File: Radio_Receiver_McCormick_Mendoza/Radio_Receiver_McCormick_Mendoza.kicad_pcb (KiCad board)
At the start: 4 copper layers, 100 x 100 mm, 243 parts, among them J1 VBAT, J10 CLK_2, J11 I_LO, J12 Q_LO, J13 I_0, J14 I_180, J15 Q_90, J16 Q_270, J17 I_RAW, J18 Conn_01x02_Female, J19 Conn_01x02_Female, J2 GND, J20 Q_RAW, J21 SDR Out, J23 VDDA, J24 CLK_0, J25 OLED, J26 +5V, J3 3.3VA, J33 XFIL_IN, J34 XFIL_OUT, J35 3.5mm_Jack, J36 +5RAW, J37 4.5V, J38 DAC_FLT, J39 VDD, J4 4.5VA, J40 DAC_FMT, J41 V_DIV, J42 VDDA/2, J45 CENTER_TAP, J46 3.5mm_Jack, J47 FIL_IN, J5 Conn_Coaxial, J6 Conn_01x02, J7 Micro_SD-TF_PUSH, J8 FIL_OUT, J9 CLK_1, SW1 RotaryEncoder_Switch_MP, SW6 09.03290.01, T1 Transformer_1P_SS, U1 TPS7A2045PDQN, U10 OPA1612AID, U11 INA821ID, U12 PCM1808PWR, U13 SN74CBT3253CDBR, U14 PCM5102A, U2 TPS7A2045PDQN, U3 TPS72733DSER, U4 Pico, U5 Si5351A-B-GT, U6 SN74AC74DR, U8 SN74CBT3253CDBR, U9 INA821ID, Y1 ASTX-H11-24.576MHZ-T

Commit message: Added netclasses for all the critical trace types
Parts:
- moved C32 15.6 mm to (103.6, 111.4)
- moved C33 15.6 mm to (100.2, 108.4)
- moved J23 15.6 mm to (100.0, 116.1)
- moved J3 15.6 mm to (96.6, 107.2)
- moved C12 15.6 mm to (104.7, 113.8)
- moved C1 15.6 mm to (104.3, 107.8)
- moved C6 15.6 mm to (99.8, 110.1)
- moved FB19 15.6 mm to (100.2, 106.8)
- moved J2 15.6 mm to (95.6, 110.8)
- moved J4 15.6 mm to (95.6, 114.6)
- moved U1 15.6 mm to (103.6, 109.8)
- moved U3 15.6 mm to (100.3, 112.7)
- moved C34 15.6 mm to (98.2, 112.8)
- moved FB18 15.6 mm to (102.7, 113.9)
- moved C22 3.69 mm to (78.4, 108.1), turned to 90 degrees

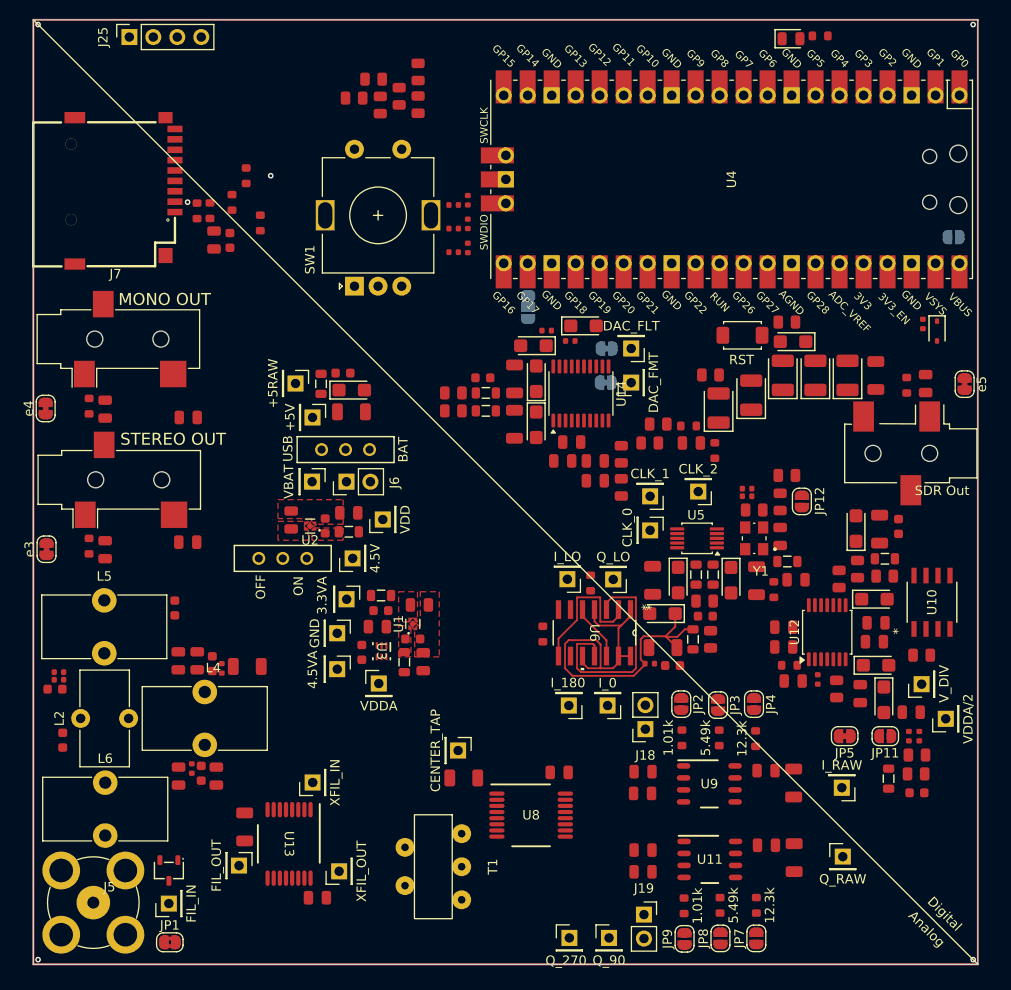
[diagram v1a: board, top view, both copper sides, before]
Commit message: Routed antenna and isolated GNDA
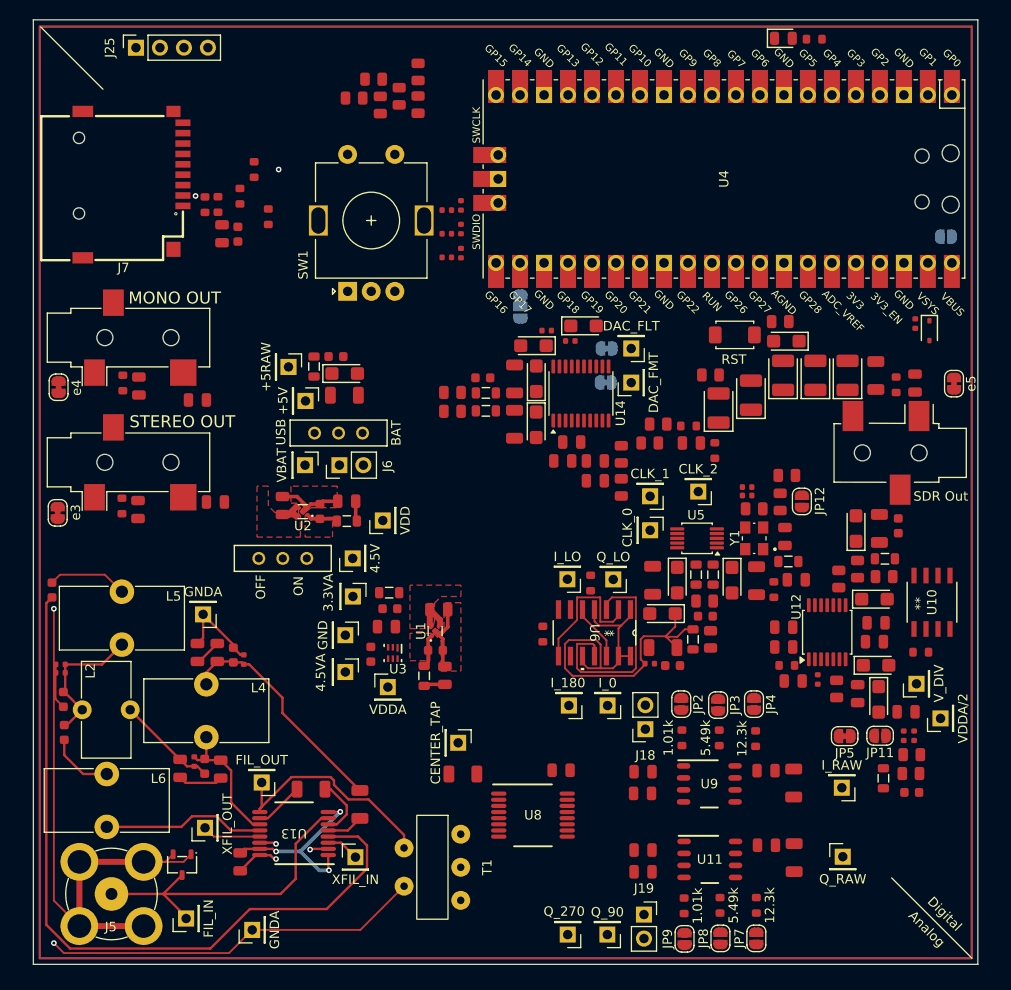
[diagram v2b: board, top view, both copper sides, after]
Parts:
- removed JP1: Jumper_NC_Small, Jumper:SolderJumper-2_P1.3mm_Bridged2Bar_RoundedPad1.0x1.5mm
- added J48: GNDA, Connector_PinHeader_2.54mm:PinHeader_1x01_P2.54mm_Vertical, F.Cu at (81.4, 108.8)
- added J49: GNDA, Connector_PinHeader_2.54mm:PinHeader_1x01_P2.54mm_Vertical, F.Cu at (86.6, 142.2)
- J7: footprint 0_Personal:TF-SMD_TF-PUSH -> Reciever_Parts:TF-SMD_TF-PUSH
- R5: value 22kΩ -> 22Ω; footprint PCM_JLCPCB:R_0805 -> PCM_JLCPCB:R_0603
- U11, U9: footprint INA821ID:D0008A_N -> Reciever_Parts:D0008A_N
- U13, U8: footprint SN74CBT3253CDBR_1-4_MUX:DB0016A_N -> Reciever_Parts:DB0016A_N
- U3: footprint TPS727-3.3V_regulator:DSE0006A -> Reciever_Parts:TS727_3.3VDSE0006A
- moved C67 18.9 mm to (98.0, 128.9), turned to 90 degrees
- moved J34 14.9 mm to (81.6, 131.4)
- moved C22 13.1 mm to (65.4, 106.2)
- moved J8 9.12 mm to (87.6, 126.6), turned to 180 degrees
- moved J33 9.10 mm to (97.5, 134.5), turned to 0 degrees
- moved C20 9.02 mm to (85.3, 135.0), turned to -90 degrees
- moved C61 8.08 mm to (92.8, 127.3), turned to 180 degrees
- moved C50 5.50 mm to (74.5, 97.7)
- moved R28 5.50 mm to (72.8, 97.3)
- moved C88 5.17 mm to (82.7, 96.9)
- moved R43 4.33 mm to (72.9, 84.3)
- moved C57 4.33 mm to (74.6, 84.6)
- moved e3 4.03 mm to (66.0, 98.0)
- moved C12 2.72 mm to (107.0, 115.3)
- moved C32 2.69 mm to (106.0, 112.6)
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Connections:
- net /ADC-24bit/VDDA/2 renamed /VREF
- net Net-(C11-Pad1) renamed /Antenna/LPF2
- net Net-(C2-Pad1) renamed /Antenna/BPF2
- net Net-(C42-Pad1) renamed /Audio DAC/OUTR_FIL
- net Net-(C43-Pad1) renamed /Audio DAC/OUTL_FIL
- net Net-(C47-Pad1) renamed /ADC-24bit/I_OUTA
- net Net-(C48-Pad1) renamed /ADC-24bit/Q_OUTA
- net Net-(C49-Pad1) renamed /Audio DAC/OUTLR
- net Net-(C59-Pad2) renamed /Audio DAC/MONO
- net Net-(C60-Pad2) renamed /Audio DAC/StereoR
- net Net-(C64-Pad1) renamed /Audio DAC/3.3VA
- net Net-(C70-Pad1) renamed /Clock Generator/3.3VA
- net Net-(C88-Pad1) renamed /Audio DAC/StereoT
- net Net-(C97-Pad1) renamed /ADC-24bit/VDDA2
- net Net-(J1-Pin_1) renamed /Power Supply/VBAT
- net Net-(J18-Pin_1) renamed /Mixer - Taloe Detector/RGI2
- net Net-(J18-Pin_2) renamed /Mixer - Taloe Detector/RGI1
- net Net-(J19-Pin_1) renamed /Mixer - Taloe Detector/RGQ2
- net Net-(J19-Pin_2) renamed /Mixer - Taloe Detector/RGQ1
- net Net-(J24-Pin_1) renamed /Clock Generator/CLK0
- net Net-(J26-Pin_1) renamed /Power Supply/5V_FIL
- net Net-(J37-Pin_1) renamed /Power Supply/4.5V
- net Net-(J4-Pin_1) renamed /Power Supply/4.5VA
- net Net-(J46-PadR) renamed /Audio DAC/MONO_OUT
- net Net-(JP11-B) renamed /ADC-24bit/Buf_IN
- net Net-(JP12-B) renamed /Clock Generator/Y1_Pin3
- net Net-(ON/OFF1-Pad1) renamed /Power Supply/ON-OFF
- net Net-(U1-EN) renamed /Power Supply/VRIN
- net Net-(U10A--) renamed /ADC-24bit/OPA_OUT
- net Net-(U10C-V+) renamed /ADC-24bit/V+
- net Net-(U12-VINL) renamed /ADC-24bit/VINL
- net Net-(U12-VINR) renamed /ADC-24bit/VINR
- net Net-(U12-VREF) renamed /ADC-24bit/VREF0
- net Net-(U13-1B1) renamed /Antenna/APF1
- net Net-(U13-1B2) renamed /Antenna/LPF1
- net Net-(U13-1B3) renamed /Antenna/BPF1
- net Net-(U13-2B1) renamed /Antenna/APF2
- net Net-(U13-2B2) renamed /Antenna/LPF3
- net Net-(U13-2B3) renamed /Antenna/BPF3
- net Net-(U14-AVDD) renamed /Audio DAC/AVDD
- net Net-(U14-CPVDD) renamed /Audio DAC/CPVDD
- net Net-(U14-OUTL) renamed /Audio DAC/OUTL
- net Net-(U14-OUTR) renamed /Audio DAC/OUTR
- net Net-(U3-OUT) renamed /Power Supply/3.3VA
- net Net-(U5-VDD) renamed /Clock Generator/CGVDD
- net Net-(U5-VDDO) renamed /Clock Generator/CGVDDO
- net Net-(U5-XA) renamed /Clock Generator/XA
- net Net-(U6A-Q) renamed /Clock Generator/JC5-12
- net Net-(U6A-~{R}) renamed /Clock Generator/JCVCC
- net Net-(Y1-TRI_STATE) renamed /Clock Generator/Y1VDD
- net Net-(e3-B) renamed /Audio DAC/JackS1
- net Net-(e5-B) renamed /ADC-24bit/JackS
- C93 pad 1: Net-(C93-Pad1) -> VDDA
- C94 pad 2: Net-(C93-Pad1) -> VDDA
- FB21 pad 2: Net-(C93-Pad1) -> VDDA
- J11 pad 1: Net-(J11-Pin_1) -> /Clock Generator/I_LO
- J12 pad 1: Net-(J12-Pin_1) -> /Clock Generator/Q_LO
- J5 pad 2: Net-(J5-Ext) -> GNDA
- R39 pad 2: Net-(J12-Pin_1) -> /Clock Generator/Q_LO
- R40 pad 1: Net-(J11-Pin_1) -> /Clock Generator/I_LO
- R52 pad 1: Net-(C93-Pad1) -> VDDA
- U6 pad 2: Net-(J12-Pin_1) -> /Clock Generator/Q_LO
- U6 pad 6: Net-(J11-Pin_1) -> /Clock Generator/I_LO
- U6 pad 8: Net-(J12-Pin_1) -> /Clock Generator/Q_LO
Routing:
- net GNDA: track 0.00 -> 129.5 mm, vias 0 -> 2
- net /Antenna/BPF1: track 0.00 -> 80.4 mm
- net /Antenna/Signal_IN: track 0.00 -> 34.9 mm
- net GND: track 0.00 -> 33.6 mm, vias 0 -> 3
- net /Antenna/LPF2: track 0.00 -> 24.6 mm
- net /Antenna/Signal_OUT: track 0.00 -> 24.1 mm
- net /Antenna/BPF3: track 0.00 -> 17.3 mm
- net /Antenna/BPF2: track 0.00 -> 15.2 mm
- net Net-(J12-Pin_1): track 14.9 -> 0.00 mm
- net /Clock Generator/Q_LO: track 0.00 -> 14.9 mm
- net /Antenna/LPF3: track 0.00 -> 14.3 mm
- net Net-(C22-Pad2): track 0.00 -> 8.49 mm
- net /Power Supply/VRIN: track 0.00 -> 7.07 mm
- net Net-(C87-Pad2): track 0.00 -> 6.95 mm
- net VDDA: track 0.00 -> 6.94 mm, vias 0 -> 1
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- added copper zone on In1.Cu, net (none)
- added copper zone on In1.Cu, net GNDA
- removed copper zone on In2.Cu, net +3.3VA
- removed copper zone on In2.Cu, net VDDA

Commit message: Resolved non-connection related DRC errors and warnings
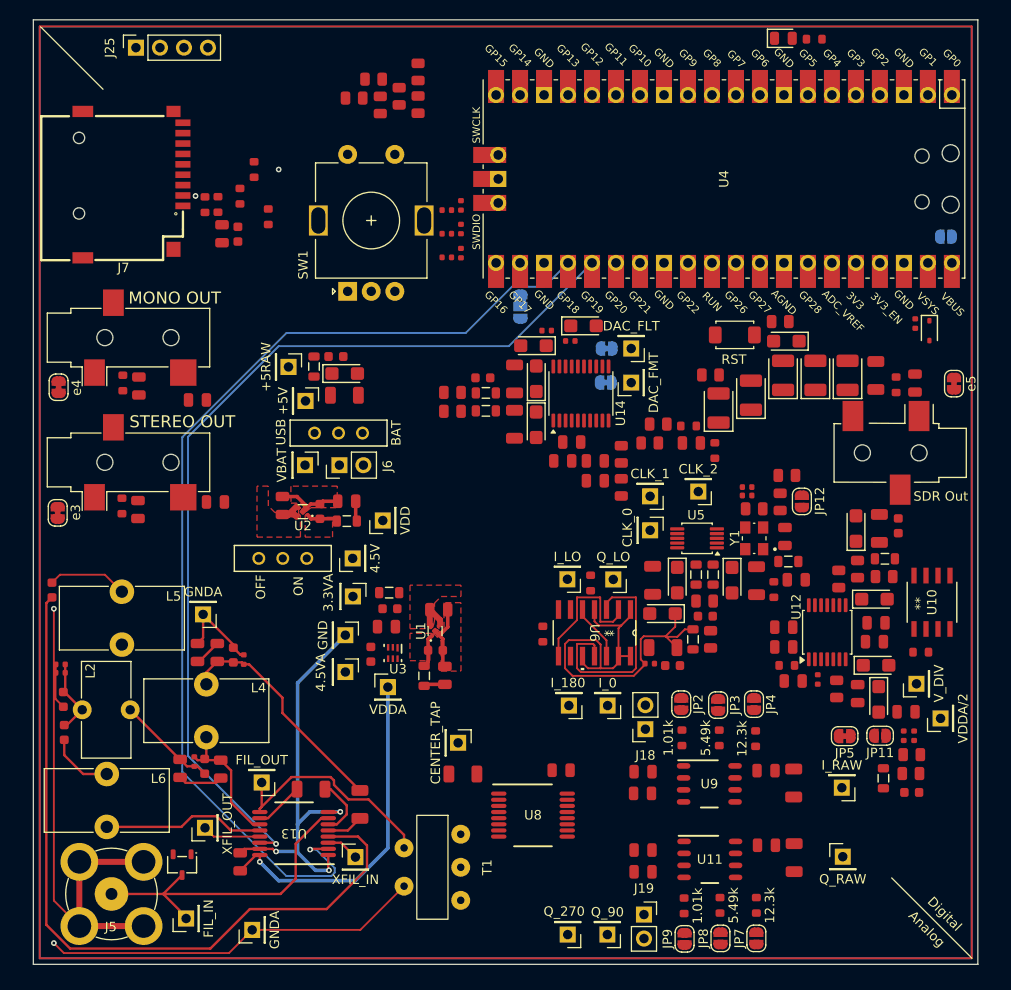
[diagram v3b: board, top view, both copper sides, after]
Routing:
- net /CTL2: track 1.96 -> 110.6 mm
- net /CTL1: track 1.78 -> 99.1 mm
- net VDDA: track 6.94 -> 38.6 mm
- net GND: track 33.6 -> 57.7 mm
- net GNDA: track 129.5 -> 120.7 mm
- net /Antenna/BPF2: track 15.2 -> 8.35 mm
- added copper zone on In1.Cu, net GND
- removed copper zone on In1.Cu, net (none)
